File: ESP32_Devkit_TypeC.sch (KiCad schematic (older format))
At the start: 57 parts, among them J1 USB_C_Receptacle_USB2.0, J2 Conn_01x19, J3 Conn_01x19, Q1 SS8050, Q2 SS8050, SW1 EN, SW2 BOOT, U1 MP2359, U2 CH340G, U3 ESP32-PICO-D4, Y1 12MHz

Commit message: Start revision F layout
The previous five revisions are not satisfactory. They have a number of
issues:

- Poor RF performance due to improper antenna placement and matching
- GPIO16 and GPIO17 are unusable, inherent problem with Pico D4
- Instability. Might be related to excessive power consumption due to
  improper antenna matching
- Changes in availability of LCSC parts

Overall those problems have prompted me to design a revision F of this
board. Most notably the ESP32 Pico D4 will be swapped for an ESP32-D0WD.
This will ensure the board actually behaves like a ESP32 DevKitC and
make it a true drop-in replacement. To ensure power and signal integrity
the new board will be a four layer one. Overall the board outline will
change slightly to allocate a suitable location for the antenna. With that
the height of the board will be closer to that of a DevKitC V1. Judging
from online listings the DevKitC V1 pinout still seems to be the most
popular one. Thus I will stick to that.
Also availability of cheap ESP32 development boards with USB Type C still
seems to be just as bad as back in 2020 when I designed the initial
revision of this board. Thus I think this new revision is a worthwhile
project.
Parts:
- removed C1: 10 nF, Capacitor_SMD:C_0402_1005Metric, symbol Device:C
- removed C12: 1uF, Capacitor_SMD:C_0402_1005Metric, symbol Device:C
- removed C13, C24: 22 uF, Capacitor_SMD:C_0603_1608Metric, symbol Device:C
- removed C14, C15, C16, C17, C18, C5, C6, C7: 100 nF, Capacitor_SMD:C_0402_1005Metric, symbol Device:C
- removed C19, C20, C21, C22: 10uF, Capacitor_SMD:C_0402_1005Metric, symbol Device:C
- removed C23, C25: 10uF, Capacitor_SMD:C_0603_1608Metric, symbol Device:C
- removed D2: B5819W, Diode_SMD:D_SOD-123, symbol Device:D_Schottky
- removed R1: 100 kR, Resistor_SMD:R_0402_1005Metric, symbol Device:R
- removed R5: 49.9kR, Resistor_SMD:R_0402_1005Metric, symbol Device:R
- removed U3: ESP32-PICO-D4, Package_ESP32:ESP32-Pico-D4, symbol RF_Module:ESP32-PICO-D4
- added C1: 22nF, Capacitor_SMD:C_0402_1005Metric, symbol Device:C_Small
- added C12, C13: 30pF, Capacitor_SMD:C_0402_1005Metric, symbol Device:C_Small
- added C14: 10uF, Capacitor_SMD:C_0402_1005Metric, symbol Device:C_Small
- added C15, C16, C17, C26: 1uF, Capacitor_SMD:C_0402_1005Metric, symbol Device:C_Small
- added C18: 3.3nF, Capacitor_SMD:C_0402_1005Metric, symbol Device:C_Small
- added C19, C5: 10nF, Capacitor_SMD:C_0402_1005Metric, symbol Device:C_Small
- added C20, C21, C24, C25, C7: 100nF, Capacitor_SMD:C_0402_1005Metric, symbol Device:C_Small
- added C22: 100pF, Capacitor_SMD:C_0402_1005Metric, symbol Device:C_Small
- added C23, C27, C28: DNP, Capacitor_SMD:C_0402_1005Metric, symbol Device:C_Small
- added C6: 22uF, Capacitor_SMD:C_0603_1608Metric, symbol Device:C_Small
- added L2: 4.7nH, Inductor_SMD:L_0603_1608Metric, symbol Device:L_Small
- added L3: 0R, Inductor_SMD:L_0402_1005Metric, symbol Device:L_Small
- added R1, R5: 100k, Resistor_SMD:R_0402_1005Metric, symbol Device:R_Small
- added R13: 20k, Resistor_SMD:R_0402_1005Metric, symbol Device:R_Small
- added U3: W25Q128JVS, Package_SO:SOIC-8_5.23x5.23mm_P1.27mm, symbol Memory_Flash:W25Q128JVS
- added U4: ESP32-D0WD, Package_DFN_QFN:QFN-48-1EP_5x5mm_P0.35mm_EP3.7x3.7mm_ThermalVias, symbol RF_Espressif:ESP32-D0WD
- added Y2: 40MHz, Crystal:Crystal_SMD_3225-4Pin_3.2x2.5mm, symbol Device:Crystal_GND24_Small
- AE1: footprint Antenna_IFA:Antenna_IFA_2.4GHz_meandered -> Antenna_IFA:Antenna_IFA_2.4GHz_meandered_mirrored
- C10, C11, C9: symbol Device:C -> Device:C_Small
- C2, C4: value 22 pF -> 22pF
- C3: value 10 uF -> 22uF 25V; symbol Device:C -> Device:C_Small; LCSC C15850 -> C45783
- C8: value 22 uF -> 22uF; symbol Device:C -> Device:C_Small
- L1: value 4.7 uH -> 10uH; footprint Inductor_SMD:L_1210_3225Metric -> Inductor_SMD:L_Taiyo-Yuden_MD-4040; LCSC C86070 -> C340393
- R10: value 100 kR -> 100k; symbol Device:R -> Device:R_Small
- R11, R12, R4: value 330 R -> 330R; symbol Device:R -> Device:R_Small
- R2, R3: value 5.1 kR -> 5.1k; symbol Device:R -> Device:R_Small
- R6: value 15 kR -> 22k; symbol Device:R -> Device:R_Small; LCSC C25756 -> C25768
- R7, R8, R9: value 5.1kR -> 5.1k; symbol Device:R -> Device:R_Small
- SW1, SW2: LCSC C115357 -> C202388
- U1: symbol Power_Management_Monolithic:MP2451 -> Power_Management_SHOUDING:SD8942
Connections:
- net +3V3: now also U2.16 (VCC), U2.4 (V3), C14.1, C15.2, C16.2, C20.1, C21.1, C22.1, C24.1, C25.1, C5.1, C6.1, C7.1, L2.1, R5.2, U4.1 (VDDA), U4.19 (VDD3P3_RTC), U4.37 (VDD3P3_CPU), U4.43 (VDDA), U4.46 (VDDA)
- net CLK: now also U3.6 (CLK), U4.31 (CLK)
- net CMD: now also U3.1 (~CS), U4.30 (CMD)
- net EN: now also C17.2, U4.9 (EN)
- net GND: now also C12.1, C13.1, C14.2, C15.1, C16.1, C17.1, C19.1, C20.2, C21.2, C22.2, C23.2, C24.2, C25.2, C26.1, C27.1, C28.1, C5.2, C6.2, C7.2, U3.4 (GND), U4.49 (GND), Y2.2, Y2.4
- net IO0: now also U4.23 (IO0)
- net IO12: now also U4.18 (IO12)
- net IO13: now also U4.20 (IO13)
- net IO14: now also U4.17 (IO14)
- net IO15: now also U4.21 (IO15)
- net IO16: now also U4.25 (IO16)
- net IO17: now also U4.27 (IO17)
- net IO18: now also U4.35 (IO18)
- net IO19: now also U4.38 (IO19)
- net IO2: now also U4.22 (IO2)
- net IO21: now also U4.42 (IO21)
- net IO22: now also U4.39 (IO22)
- net IO23: now also U4.36 (IO23)
- net IO25: now also U4.14 (IO25)
- net IO26: now also U4.15 (IO26)
- net IO27: now also U4.16 (IO27)
- net IO32: now also U4.12 (IO32)
- net IO33: now also U4.13 (IO33)
- net IO34: now also U4.10 (IO34)
- net IO35: now also U4.11 (IO35)
- net IO4: now also U4.24 (IO4)
- net IO5: now also U4.34 (IO5)
- net RXD: now also U4.40 (U0RXD/IO3)
- net SD0: now also U3.5 (DI(IO0)), U4.32 (SD0)
- net SD1: now also U3.2 (DO(IO1)), U4.33 (SD1)
- net SD2: now also U3.3 (IO2), U4.29 (SD3)
- net SD3: now also U3.7 (IO3), U4.28 (SD2)
- net TXD: now also U4.41 (U0TXD/IO1)
- net VBUS: no longer U2.16 (VCC)
- net VCC: now also R1.2
- net VN: now also U4.8 (SENSOR_VN)
- net VP: now also U4.5 (SENSOR_VP)
- net at AE1.1 (A): now also C28.2, L3.2
- net at U1.1 (BST): now also C1.2
- net at C9.2, R6.1, U1.3 (FB): now also R5.1
- net at U1.4 (EN): now also R1.1
- net at L1.1, U1.6 (SW): now also C1.1
- new net: C27.2, L3.1, U4.2 (LNA_IN)
- new net: C23.1, L2.2, U4.3 (VDDA3P3), U4.4 (VDDA3P3)
- new net: C12.2, U4.44 (XTAL_N), Y2.1
- new net: C13.2, U4.45 (XTAL_P), Y2.3
- new net: C18.2, R13.1, U4.47 (CAP2)
- new net: C18.1, C19.2, R13.2, U4.48 (CAP1)
- new net VDD_SDIO: C26.2, U3.8 (VCC), U4.26 (VDD_SDIO)
- no-connect marks 2 -> 8
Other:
- moved on the sheet: AE1, C3, C8, D3, J2, J3, R10, R6

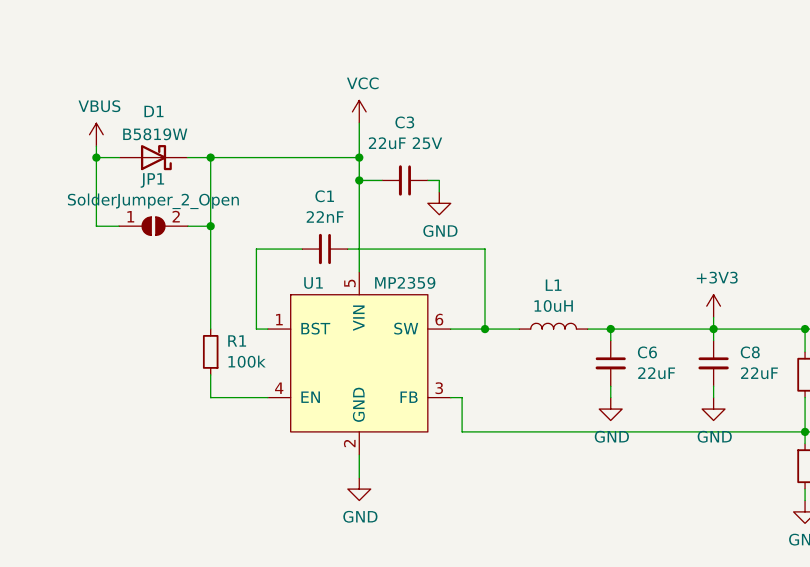
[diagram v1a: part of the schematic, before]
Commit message: Layout primary step-down converter
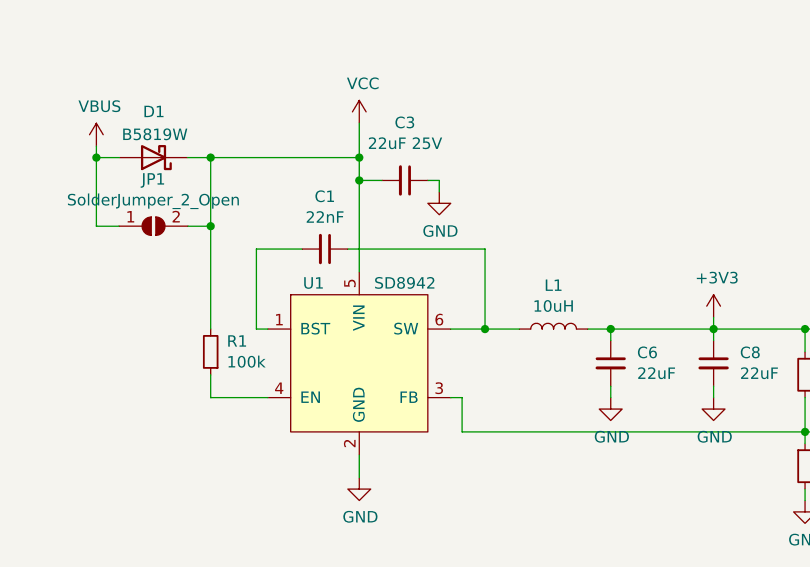
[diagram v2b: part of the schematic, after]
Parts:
- U1: value MP2359 -> SD8942; LCSC C14259 -> C250795
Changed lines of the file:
@@
 P 2200 5150
 F 0 "U1" H 2000 5500 50  0000 C CNN
-F 1 "MP2359" H 2400 5500 50  0000 C CNN
+F 1 "SD8942" H 2400 5500 50  0000 C CNN
 F 2 "Package_TO_SOT_SMD:SOT-23-6" H 2200 6100 50  0001 C CNN
-F 3 "https://datasheet.lcsc.com/szlcsc/Monolithic-Power-Systems-MPS-MP2451DT-LF-Z_C14123.pdf" H 2200 6100 50  0001 C CNN
-F 4 "C14259" H 2200 5150 50  0001 C CNN "LCSC"
+F 3 "https://datasheet.lcsc.com/szlcsc/1808081634_SHOUDING-SD8942_C250795.pdf" H 2200 6100 50  0001 C CNN
+F 4 "C250795" H 2200 5150 50  0001 C CNN "LCSC"
 	1    2200 5150
 	1    0    0    -1

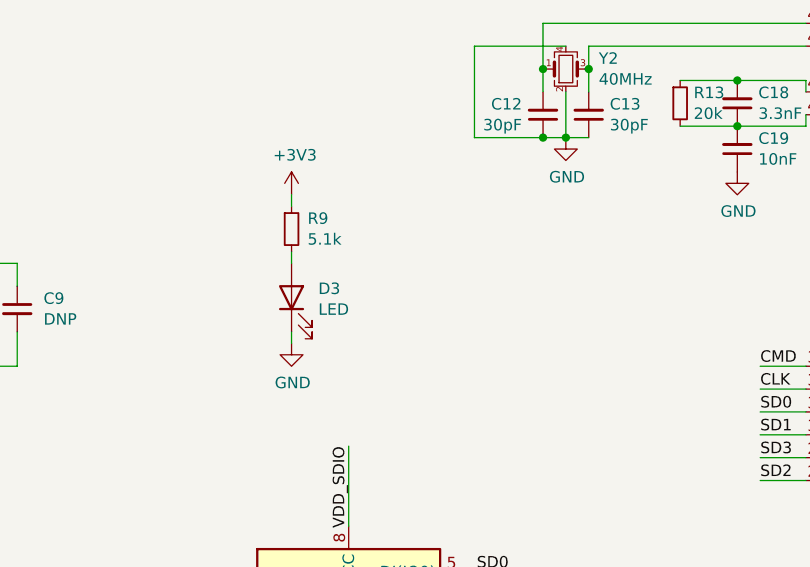
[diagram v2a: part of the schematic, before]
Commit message: Layout WiP
ESP32 should be rotated by 90°, save current layouting progress
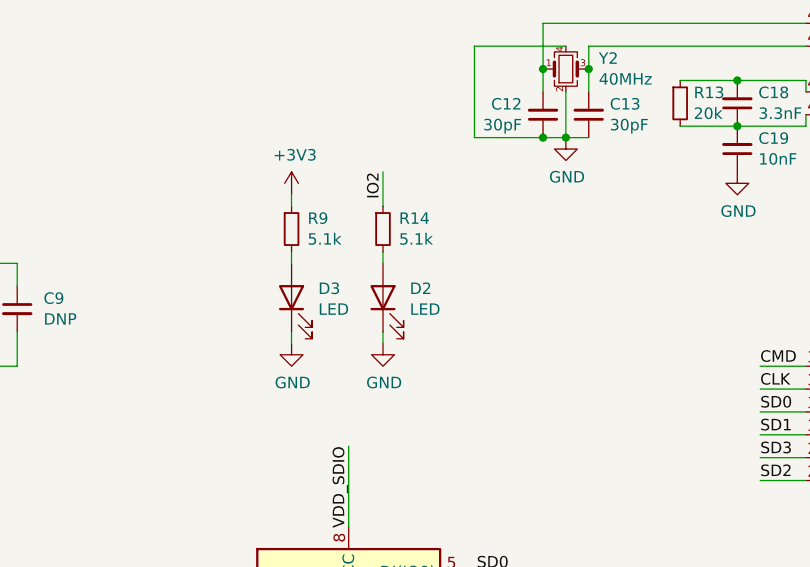
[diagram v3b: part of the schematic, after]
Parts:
- added D2: LED, LED_SMD:LED_0603_1608Metric_Castellated, symbol Device:LED
- added R14: 5.1k, Resistor_SMD:R_0402_1005Metric, symbol Device:R_Small
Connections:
- net GND: now also D2.1 (K)
- net IO2: now also R14.1
- new net: D2.2 (A), R14.2
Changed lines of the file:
@@
 	-1   0    0    1
 $EndComp
+$Comp
+L Device:LED D2
+U 1 1 62A908B3
+P 6200 5150
+F 0 "D2" V 6239 5033 50  0000 R CNN
+F 1 "LED" V 6148 5033 50  0000 R CNN
+F 2 "LED_SMD:LED_0603_1608Metric_Castellated" H 6200 5150 50  0001 C CNN
+F 3 "~" H 6200 5150 50  0001 C CNN
+F 4 "C2286" V 6200 5150 50  0001 C CNN "LCSC"
+	1    6200 5150
+	0    -1   -1   0
+$EndComp
+$Comp
+L Device:R_Small R14
+U 1 1 62A908BA
+P 6200 4850
+F 0 "R14" H 6270 4896 50  0000 L CNN
+F 1 "5.1k" H 6270 4805 50  0000 L CNN
+F 2 "Resistor_SMD:R_0402_1005Metric" V 6130 4850 50  0001 C CNN
+F 3 "~" H 6200 4850 50  0001 C CNN
+F 4 " C25905" H 6200 4850 50  0001 C CNN "LCSC"
+	1    6200 4850
+	1    0    0    -1
+$EndComp
+$Comp
+L power:GND #PWR0146
+U 1 1 62A908C0
+P 6200 5350
+F 0 "#PWR0146" H 6200 5100 50  0001 C CNN
+F 1 "GND" H 6205 5177 50  0000 C CNN
+F 2 "" H 6200 5350 50  0001 C CNN
+F 3 "" H 6200 5350 50  0001 C CNN
+	1    6200 5350
+	1    0    0    -1
+$EndComp
+Wire Wire Line
+	6200 5350 6200 5300
+Wire Wire Line
+	6200 5000 6200 4950
+Text Label 6200 4600 3    50   ~ 0
+IO2
+Wire Wire Line
+	6200 4600 6200 4750
 $EndSCHEMATC
